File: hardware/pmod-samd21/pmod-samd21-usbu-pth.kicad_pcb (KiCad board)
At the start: 2 copper layers, 18.2 x 31.1 mm, 19 parts, among them J1 PMOD-2x6-MALE, J2 PMOD-2x6-FEMALE, J3 USB_B_Micro, Q1 2N7002PW, U1 ATSAMD21G-A, Y1 32.768kHz

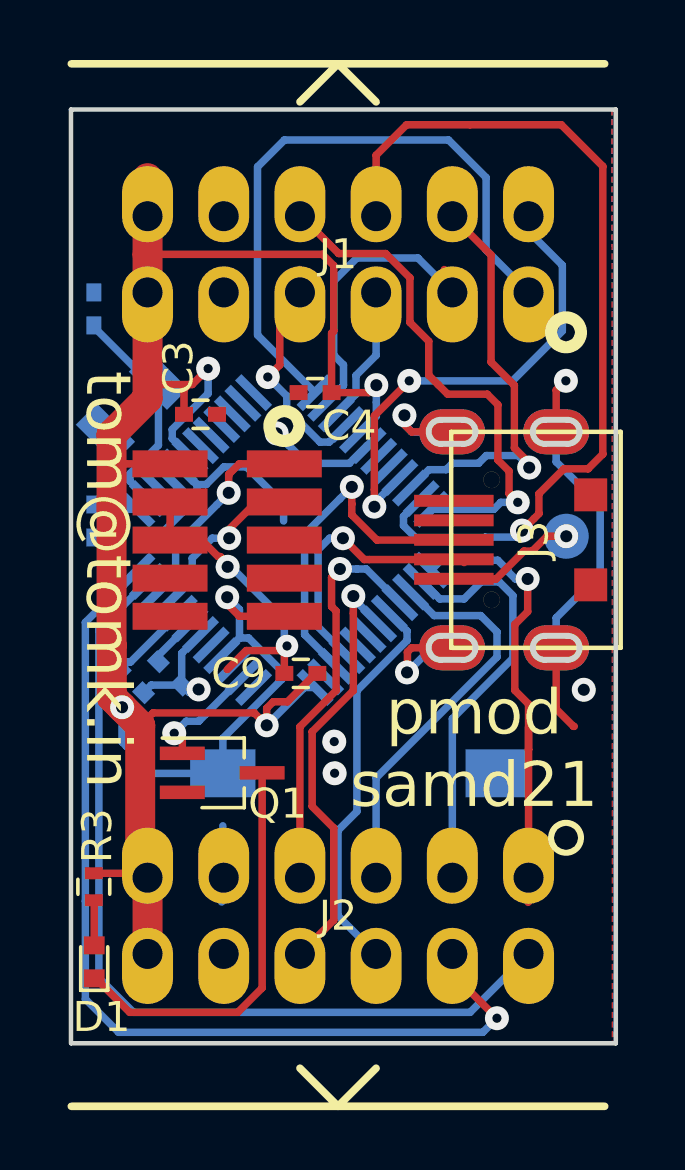
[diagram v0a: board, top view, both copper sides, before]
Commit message: pmod-samd21 : changes for seeed studio opl fabrication
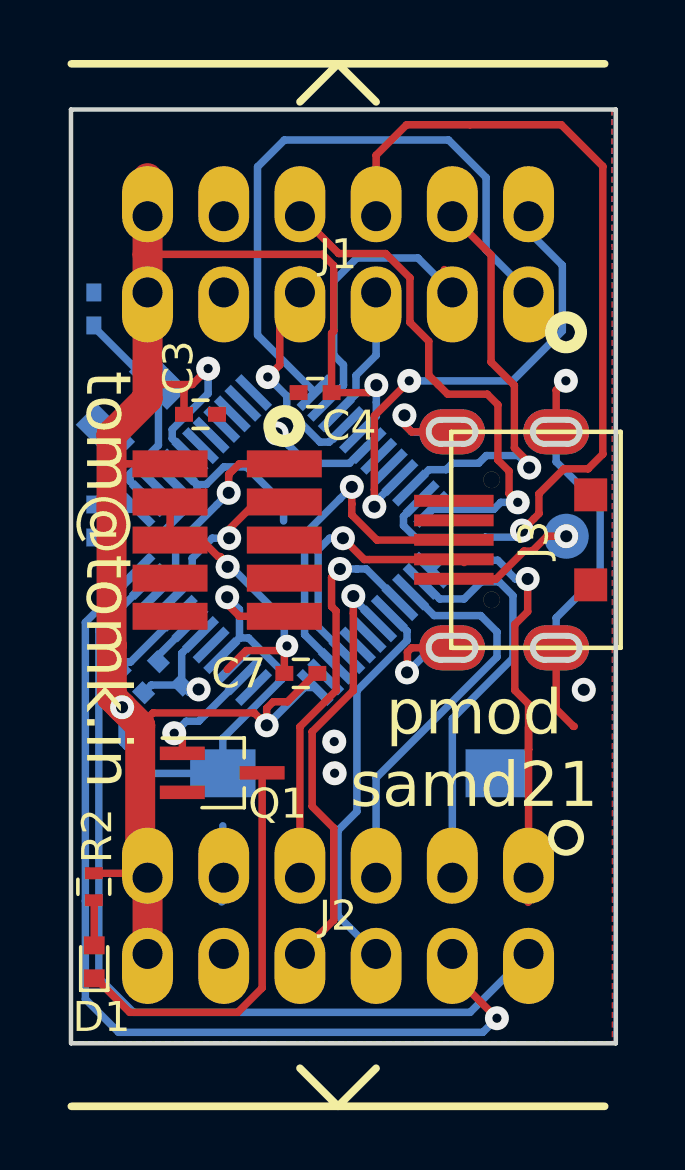
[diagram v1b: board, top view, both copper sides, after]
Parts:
- C7: renamed from C9; value 0.1uF -> 1uF
- renumbered JP2 to J4, R3 to R2
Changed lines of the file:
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@@
   (general
     (thickness 1.6)
-    (drawings 7)
+    (drawings 9)
     (tracks 402)
     (zones 0)
@@
     (32 B.Adhes user hide)
     (33 F.Adhes user hide)
-    (34 B.Paste user)
-    (35 F.Paste user)
+    (34 B.Paste user hide)
+    (35 F.Paste user hide)
     (36 B.SilkS user)
-    (37 F.SilkS user)
+    (37 F.SilkS user hide)
     (38 B.Mask user)
     (39 F.Mask user)
-    (40 Dwgs.User user hide)
+    (40 Dwgs.User user)
     (41 Cmts.User user hide)
     (42 Eco1.User user hide)
@@
     (solder_mask_min_width 0.25)
     (aux_axis_origin 142.7607 166)
+    (grid_origin 142.748 166)
     (visible_elements 7FFFFFFF)
     (pcbplotparams
@@
   (module tom-connectors:CONN_1.27_2x5 (layer F.Cu)
     (at 147.955 149.225 270)
-    (fp_text reference JP2 (at 0 4.445 90) (layer F.SilkS) hide
+    (fp_text reference J4 (at 0 4.445 90) (layer F.SilkS) hide
       (effects (font (size 1 1) (thickness 0.15)))
     )
@@
     (tags "capacitor 0402")
     (attr smd)
-    (fp_text reference C9 (at 2.074 0 180) (layer F.SilkS)
-      (effects (font (size 1 1) (thickness 0.15)))
-    )
-    (fp_text value 0.1uF (at 0 1.27 180) (layer F.Fab) hide
+    (fp_text reference C7 (at 2.074 0 180) (layer F.SilkS)
+      (effects (font (size 1 1) (thickness 0.15)))
+    )
+    (fp_text value 1uF (at 0 1.27 180) (layer F.Fab) hide
       (effects (font (size 1 1) (thickness 0.15)))
     )
@@
     (tags "resistor 0402")
     (attr smd)
-    (fp_text reference R3 (at 1.7018 0.1143 90) (layer F.SilkS)
+    (fp_text reference R2 (at 1.7018 0.1143 90) (layer F.SilkS)
       (effects (font (size 1 1) (thickness 0.15)))
     )
@@
       (net 30 "Net-(J3-Pad1)"))
   )
+  (dimension 18.415 (width 0.3) (layer Dwgs.User)
+    (gr_text "18.415 mm" (at 151.9555 173.18) (layer Dwgs.User)
+      (effects (font (size 1.5 1.5) (thickness 0.3)))
+    )
+    (feature1 (pts (xy 161.163 164.73) (xy 161.163 171.666421)))
+    (feature2 (pts (xy 142.748 164.73) (xy 142.748 171.666421)))
+    (crossbar (pts (xy 142.748 171.08) (xy 161.163 171.08)))
+    (arrow1a (pts (xy 161.163 171.08) (xy 160.036496 171.666421)))
+    (arrow1b (pts (xy 161.163 171.08) (xy 160.036496 170.493579)))
+    (arrow2a (pts (xy 142.748 171.08) (xy 143.874504 171.666421)))
+    (arrow2b (pts (xy 142.748 171.08) (xy 143.874504 170.493579)))
+  )
+  (dimension 31.115 (width 0.3) (layer Dwgs.User)
+    (gr_text "31.115 mm" (at 168.978 150.4425 90) (layer Dwgs.User)
+      (effects (font (size 1.5 1.5) (thickness 0.3)))
+    )
+    (feature1 (pts (xy 160.528 134.885) (xy 167.464421 134.885)))
+    (feature2 (pts (xy 160.528 166) (xy 167.464421 166)))
+    (crossbar (pts (xy 166.878 166) (xy 166.878 134.885)))
+    (arrow1a (pts (xy 166.878 134.885) (xy 167.464421 136.011504)))
+    (arrow1b (pts (xy 166.878 134.885) (xy 166.291579 136.011504)))
+    (arrow2a (pts (xy 166.878 166) (xy 167.464421 164.873496)))
+    (arrow2b (pts (xy 166.878 166) (xy 166.291579 164.873496)))
+  )
   (gr_line (start 142.748 134.874) (end 142.748 166) (layer Edge.Cuts) (width 0.15))
